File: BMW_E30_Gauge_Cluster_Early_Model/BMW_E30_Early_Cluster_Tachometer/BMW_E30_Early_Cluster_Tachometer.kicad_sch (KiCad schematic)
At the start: 0 parts

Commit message: Started Tach and EG Schematics
Started pinouts for tachometer and EG schematics. Also made a notation update to the Nexus schematic, removed a TODO that was completed.
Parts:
- added D1: 1N4004, Diode_THT:D_DO-41_SOD81_P10.16mm_Horizontal, symbol Diode:1N4005
- added J1: Conn_01x11_Socket, symbol Connector:Conn_01x11_Socket
- added J2: To EG, symbol Connector:Conn_01x05_Socket
- added Q1: BC547C, Package_TO_SOT_THT:TO-92_Inline, symbol Transistor_BJT:BC547
- added R1: 10k, symbol Device:R
- added R2: 20R, symbol Device:R
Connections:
- new net: J1.11 (Pin_11), J2.2 (Pin_2)
- new net: J1.7 (Pin_7), J2.1 (Pin_1)
- new net: D1.1 (K), R2.2
- new net: Q1.2 (B), R1.2
- new net: J2.3 (Pin_3), Q1.1 (C)
- new net +12V T15: D1.2 (A), J1.1 (Pin_1), J2.4 (Pin_4)
- new net +12V T15_ACC: J1.5 (Pin_5)
- new net +12V T30: J1.10 (Pin_10)
- new net +5V: J1.9 (Pin_9)
- new net Cylinder_count: J1.6 (Pin_6), R1.1
- new net GNDPWR: J1.3 (Pin_3), J2.5 (Pin_5), Q1.3 (E)
- new net VCC_T15: R2.1
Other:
- note added: "Cylinder count"
- note added: "Distance pulse"
- note added: "Engine speed input"
- note added: "Fuel rate input"
- note added: "Speed pulse"
- note added: "Wheel speed output"
- company: (none) -> Reagan Ansel
- title: (none) -> BMW E30 Gauge Cluster Tachometer Schematic

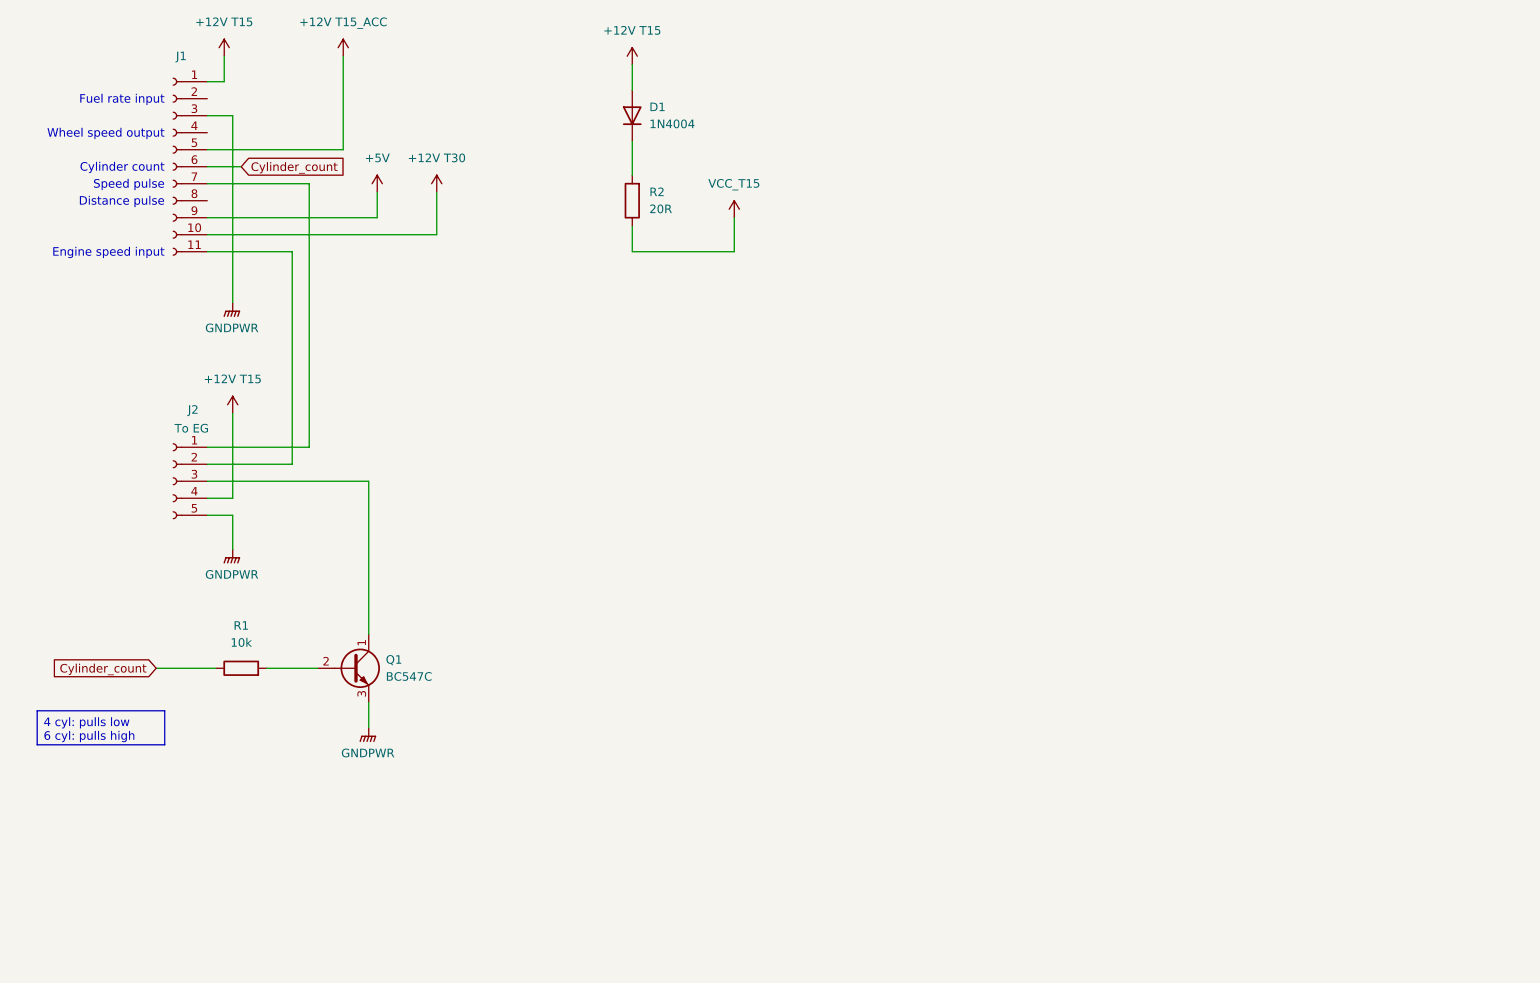
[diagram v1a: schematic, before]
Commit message: Tachometer Schematic Completed
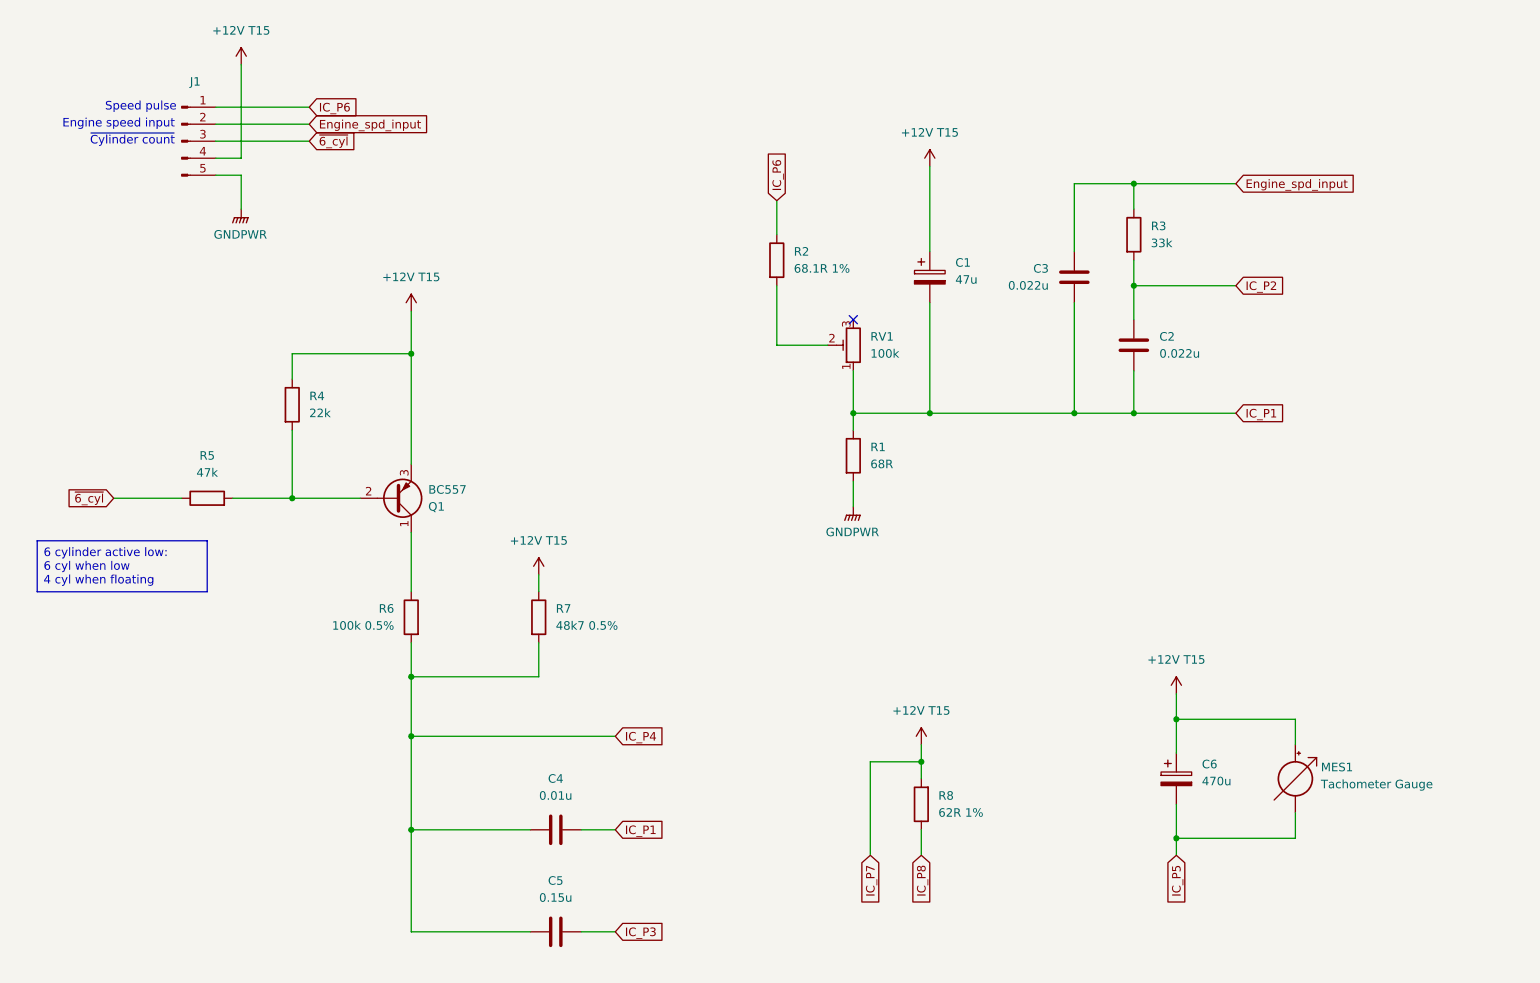
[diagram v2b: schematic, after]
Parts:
- removed D1: 1N4004, Diode_THT:D_DO-41_SOD81_P10.16mm_Horizontal, symbol Diode:1N4005
- removed J1: Conn_01x11_Socket, symbol Connector:Conn_01x11_Socket
- removed J2: To EG, symbol Connector:Conn_01x05_Socket
- removed Q1: BC547C, Package_TO_SOT_THT:TO-92_Inline, symbol Transistor_BJT:BC547
- added C1: 47u, symbol Device:C_Polarized
- added C2, C3: 0.022u, symbol Device:C
- added C4: 0.01u, symbol Device:C
- added C5: 0.15u, symbol Device:C
- added C6: 470u, Capacitor_THT:CP_Axial_L25.0mm_D10.0mm_P30.00mm_Horizontal, symbol Device:C_Polarized
- added J1: Conn_01x05_Pin, symbol Connector:Conn_01x05_Pin
- added MES1: Tachometer Gauge, symbol Device:Galvanometer
- added Q1: BC557, Package_TO_SOT_THT:TO-92_Inline, symbol Transistor_BJT:BC557
- added R3: 33k, symbol Device:R
- added R4: 22k, symbol Device:R
- added R5: 47k, symbol Device:R
- added R6: 100k 0.5%, symbol Device:R
- added R7: 48k7 0.5%, symbol Device:R
- added R8: 62R 1%, symbol Device:R
- added RV1: 100k, Potentiometer_THT:Potentiometer_Runtron_RM-065_Vertical, symbol Device:R_Potentiometer_Trim
- R1: value 10k -> 68R
- R2: value 20R -> 68.1R 1%
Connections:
- net +12V T15: now also C1.1, C6.1, J1.4 (Pin_4), MES1.2 (+), Q1.3 (E), R4.1, R7.1, R8.2
- net GNDPWR: now also R1.2, J1.5 (Pin_5)
- net at R2.2: now also RV1.2
- net Cylinder_count renamed IC_P1
- net IC_P1: now also C1.2, C2.2, C3.2, C4.1, RV1.1
- net VCC_T15 renamed IC_P6
- net IC_P6: now also J1.1 (Pin_1)
- new net: Q1.1 (C), R6.1
- new net: Q1.2 (B), R4.2, R5.2
- new net Engine_spd_input: C3.1, J1.2 (Pin_2), R3.1
- new net IC_P2: C2.1, R3.2
- new net IC_P3: C5.1
- new net IC_P4: C4.2, C5.2, R6.2, R7.2
- new net IC_P5: C6.2, MES1.1 (-)
- new net IC_P8: R8.1
- new net ~{6_cyl}: J1.3 (Pin_3), R5.1
- no-connect marks 0 -> 1
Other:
- note added: "~{Cylinder count}"
- note removed: "Cylinder count"
- note removed: "Distance pulse"
- note removed: "Fuel rate input"
- note removed: "Wheel speed output"
- title: BMW E30 Gauge Cluster Tachometer Schematic -> BMW E30 Gauge Cluster Tachometer Gauge

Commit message: Added IC Symbol
Added symbol for SN29736P to the BMW IC's library and to the schematic.
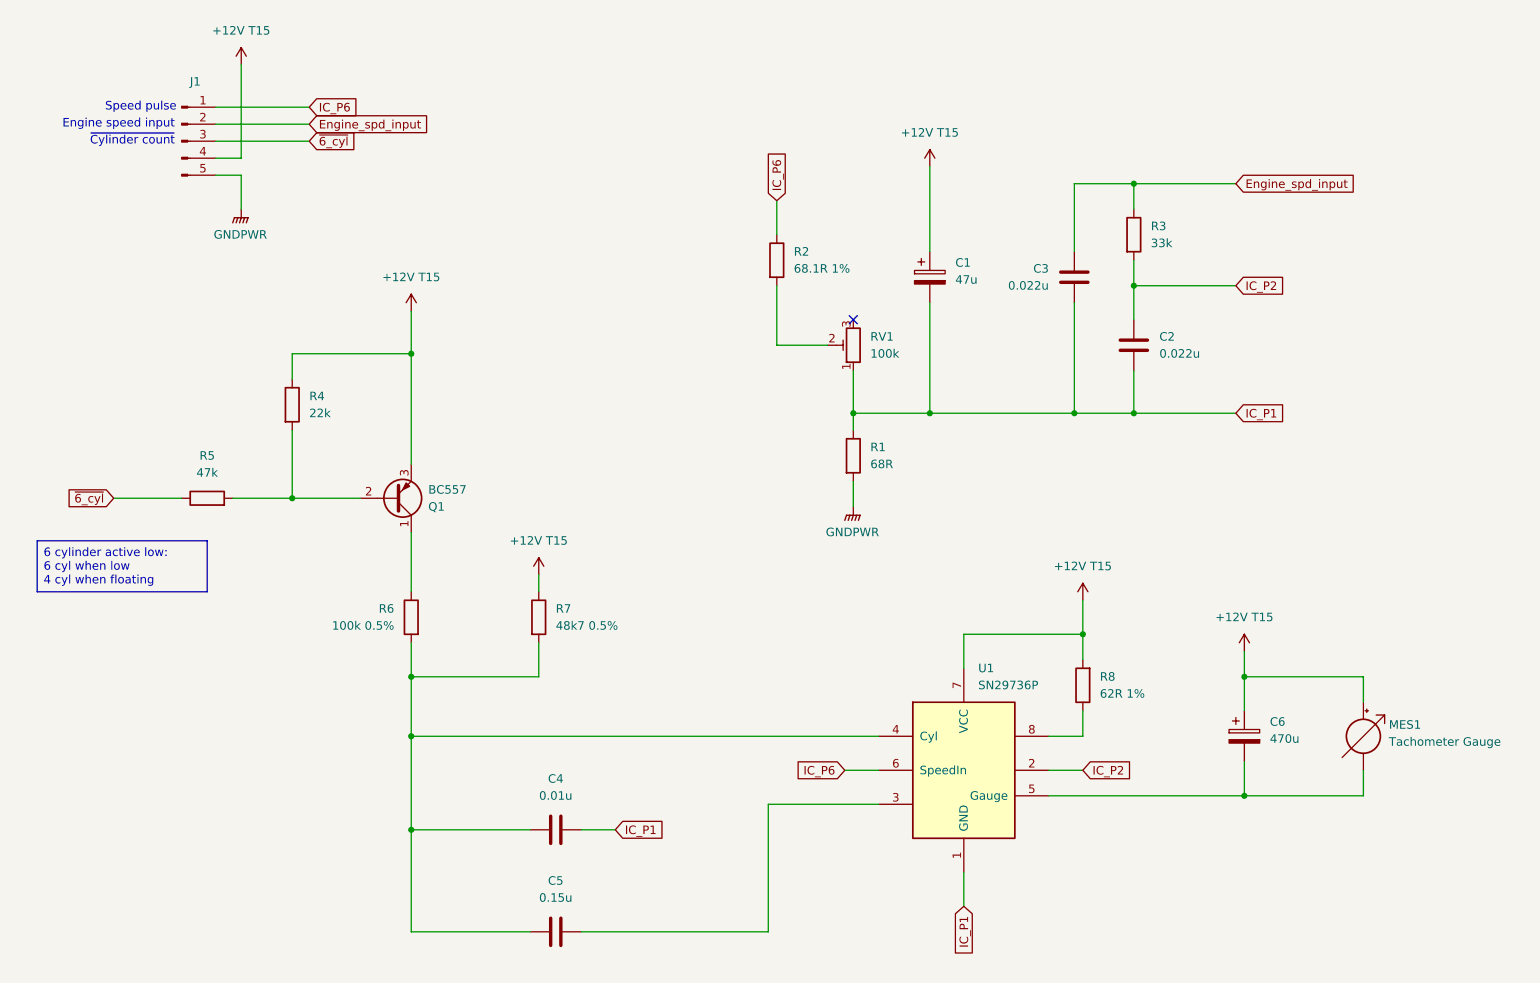
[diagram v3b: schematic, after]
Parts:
- added U1: SN29736P, Package_DIP:DIP-8_W7.62mm_Socket_LongPads, symbol BMW_ICs:SN29736P
- Q1: footprint Package_TO_SOT_THT:TO-92_Inline -> Package_TO_SOT_THT:TO-92_Wide
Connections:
- net +12V T15: now also U1.7 (VCC)
- net IC_P1: now also U1.1 (GND)
- net IC_P2: now also U1.2
- net IC_P6: now also U1.6 (SpeedIn)
- net IC_P3: no longer names the net of C5.1
- net IC_P3: now also U1.3
- net IC_P4: no longer names the net of C4.2, C5.2, R6.2, R7.2
- net IC_P4: now also U1.4 (Cyl)
- net IC_P5: no longer names the net of C6.2, MES1.1 (-)
- net IC_P5: now also U1.5 (Gauge)
- net IC_P8: no longer names the net of R8.1
- net IC_P8: now also U1.8
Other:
- moved on the sheet: C6, MES1, R8

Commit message: Component Placement on Tach Board
Completed component placement part of layout for the tachometer pcb. All footprints are created and locations set. Final step is trace layout.
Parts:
- C1: footprint (none) -> Capacitor_THT:CP_Axial_L11.0mm_D6.0mm_P18.00mm_Horizontal
- C2, C3, C5: footprint (none) -> Capacitor_THT:C_Axial_L12.0mm_D6.5mm_P15.00mm_Horizontal
- C4: footprint (none) -> Capacitor_THT:C_Disc_D5.0mm_W2.5mm_P5.00mm
- J1: footprint (none) -> BMW_Cluster_Connectors:EG_Tach_Pins
- MES1: footprint (none) -> BMW_Cluster_Connectors:Connector_Tach
- R1: footprint (none) -> Resistor_THT:R_Axial_DIN0411_L9.9mm_D3.6mm_P15.24mm_Horizontal
- R2, R3, R4, R5, R6, R7: footprint (none) -> Resistor_THT:R_Axial_DIN0207_L6.3mm_D2.5mm_P7.62mm_Horizontal
- R8: footprint (none) -> Resistor_THT:R_Axial_DIN0309_L9.0mm_D3.2mm_P15.24mm_Horizontal
- RV1: footprint Potentiometer_THT:Potentiometer_Runtron_RM-065_Vertical -> Potentiometer_THT:Potentiometer_Piher_PT-10-V10_Vertical
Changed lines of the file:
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@@
 			)
 		)
-		(property "Footprint" ""
+		(property "Footprint" "Resistor_THT:R_Axial_DIN0207_L6.3mm_D2.5mm_P7.62mm_Horizontal"
 			(at 90.932 107.95 90)
 			(effects
@@
 			)
 		)
-		(property "Footprint" ""
+		(property "Footprint" "Resistor_THT:R_Axial_DIN0207_L6.3mm_D2.5mm_P7.62mm_Horizontal"
 			(at 75.438 107.95 90)
 			(effects
@@
 			)
 		)
-		(property "Footprint" ""
+		(property "Footprint" "Resistor_THT:R_Axial_DIN0207_L6.3mm_D2.5mm_P7.62mm_Horizontal"
 			(at 54.102 76.2 90)
 			(effects
@@
 			)
 		)
-		(property "Footprint" ""
+		(property "Footprint" "BMW_Cluster_Connectors:Connector_Tach"
 			(at 215.9 123.19 90)
 			(effects
@@
 			)
 		)
-		(property "Footprint" ""
+		(property "Footprint" "BMW_Cluster_Connectors:EG_Tach_Pins"
 			(at 39.37 36.83 0)
 			(effects
@@
 			)
 		)
-		(property "Footprint" ""
+		(property "Footprint" "Resistor_THT:R_Axial_DIN0207_L6.3mm_D2.5mm_P7.62mm_Horizontal"
 			(at 43.18 91.948 90)
 			(effects
@@
 			)
 		)
-		(property "Footprint" ""
+		(property "Footprint" "Capacitor_THT:C_Axial_L12.0mm_D6.5mm_P15.00mm_Horizontal"
 			(at 91.44 155.9052 0)
 			(effects
@@
 			)
 		)
-		(property "Footprint" ""
+		(property "Footprint" "Resistor_THT:R_Axial_DIN0207_L6.3mm_D2.5mm_P7.62mm_Horizontal"
 			(at 179.832 50.8 90)
 			(effects
@@
 			)
 		)
-		(property "Footprint" ""
+		(property "Footprint" "Capacitor_THT:C_Disc_D5.0mm_W2.5mm_P5.00mm"
 			(at 91.44 140.6652 0)
 			(effects
@@
 			)
 		)
-		(property "Footprint" ""
+		(property "Footprint" "Resistor_THT:R_Axial_DIN0309_L9.0mm_D3.2mm_P15.24mm_Horizontal"
 			(at 175.768 118.11 90)
 			(effects
@@
 			)
 		)
-		(property "Footprint" ""
+		(property "Footprint" "Capacitor_THT:C_Axial_L12.0mm_D6.5mm_P15.00mm_Horizontal"
 			(at 171.7548 60.96 0)
 			(effects
@@
 			)
 		)
-		(property "Footprint" ""
+		(property "Footprint" "Capacitor_THT:CP_Axial_L11.0mm_D6.0mm_P18.00mm_Horizontal"
 			(at 152.0952 60.96 0)
 			(effects
@@
 			)
 		)
-		(property "Footprint" ""
+		(property "Footprint" "Capacitor_THT:C_Axial_L12.0mm_D6.5mm_P15.00mm_Horizontal"
 			(at 182.5752 71.12 0)
 			(effects
@@
 			)
 		)
-		(property "Footprint" ""
+		(property "Footprint" "Resistor_THT:R_Axial_DIN0411_L9.9mm_D3.6mm_P15.24mm_Horizontal"
 			(at 137.922 83.82 90)
 			(effects
@@
 			)
 		)
-		(property "Footprint" ""
+		(property "Footprint" "Resistor_THT:R_Axial_DIN0207_L6.3mm_D2.5mm_P7.62mm_Horizontal"
 			(at 126.492 54.61 90)
 			(effects
@@
 			)
 		)
-		(property "Footprint" "Potentiometer_THT:Potentiometer_Runtron_RM-065_Vertical"
+		(property "Footprint" "Potentiometer_THT:Potentiometer_Piher_PT-10-V10_Vertical"
 			(at 139.7 67.31 0)
 			(effects

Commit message: Update Schematic PDFs
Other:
- company: Reagan Ansel -> Reans
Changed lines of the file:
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@@
 	(title_block
 		(title "BMW E30 Gauge Cluster Tachometer Gauge")
-		(company "Reagan Ansel")
-		(comment 1 "All resistors are 5% tolorance unless otherwise noted")
+		(date "2026-06-03")
+		(rev "0")
+		(company "Reans")
+		(comment 1 "Reagan Ansel")
+		(comment 2 "All resistors are 5% tolorance unless otherwise noted")
 	)
 	(text "Speed pulse"
@@
 		)
 		(instances
-			(project "BMW_E30_Early_Cluster_EG"
+			(project "BMW_E30_Early_Cluster_Tachometer"
 				(path "/87822f16-f981-4ad2-bfeb-178300c0bdac"
 					(reference "#PWR07")
@@
 		)
 		(instances
-			(project ""
+			(project "BMW_E30_Early_Cluster_Tachometer"
 				(path "/87822f16-f981-4ad2-bfeb-178300c0bdac"
 					(reference "MES1")
@@
 		)
 		(instances
-			(project ""
+			(project "BMW_E30_Early_Cluster_Tachometer"
 				(path "/87822f16-f981-4ad2-bfeb-178300c0bdac"
 					(reference "J1")
@@
 		)
 		(instances
-			(project "BMW_E30_Early_Cluster_EG"
+			(project "BMW_E30_Early_Cluster_Tachometer"
 				(path "/87822f16-f981-4ad2-bfeb-178300c0bdac"
 					(reference "#PWR01")
@@
 		)
 		(instances
-			(project ""
+			(project "BMW_E30_Early_Cluster_Tachometer"
 				(path "/87822f16-f981-4ad2-bfeb-178300c0bdac"
 					(reference "Q1")
@@
 		)
 		(instances
-			(project "BMW_E30_Early_Cluster_EG"
+			(project "BMW_E30_Early_Cluster_Tachometer"
 				(path "/87822f16-f981-4ad2-bfeb-178300c0bdac"
 					(reference "#PWR06")
@@
 		)
 		(instances
-			(project "BMW_E30_Early_Cluster_EG"
+			(project "BMW_E30_Early_Cluster_Tachometer"
 				(path "/87822f16-f981-4ad2-bfeb-178300c0bdac"
 					(reference "R3")
@@
 		)
 		(instances
-			(project "BMW_E30_Early_Cluster_EG"
+			(project "BMW_E30_Early_Cluster_Tachometer"
 				(path "/87822f16-f981-4ad2-bfeb-178300c0bdac"
 					(reference "C3")
@@
 		)
 		(instances
-			(project ""
+			(project "BMW_E30_Early_Cluster_Tachometer"
 				(path "/87822f16-f981-4ad2-bfeb-178300c0bdac"
 					(reference "C1")
@@
 		)
 		(instances
-			(project ""
+			(project "BMW_E30_Early_Cluster_Tachometer"
 				(path "/87822f16-f981-4ad2-bfeb-178300c0bdac"
 					(reference "U1")
@@
 		)
 		(instances
-			(project ""
+			(project "BMW_E30_Early_Cluster_Tachometer"
 				(path "/87822f16-f981-4ad2-bfeb-178300c0bdac"
 					(reference "C2")
@@
 		)
 		(instances
-			(project ""
+			(project "BMW_E30_Early_Cluster_Tachometer"
 				(path "/87822f16-f981-4ad2-bfeb-178300c0bdac"
 					(reference "R1")
@@
 		)
 		(instances
-			(project "BMW_E30_Early_Cluster_EG"
+			(project "BMW_E30_Early_Cluster_Tachometer"
 				(path "/87822f16-f981-4ad2-bfeb-178300c0bdac"
 					(reference "R2")
@@
 		)
 		(instances
-			(project ""
+			(project "BMW_E30_Early_Cluster_Tachometer"
 				(path "/87822f16-f981-4ad2-bfeb-178300c0bdac"
 					(reference "RV1")
@@
 	)
 	(embedded_fonts no)
+	(embedded_files
+		(file
+			(name "reans_sheet_template.kicad_wks")
+			(type worksheet)
+			(data |KLUv/WD/Cu0XAPbhaSEA1TZqxSYVNDoEMnCBWkUAFLHYT8LfLc64wmSW/n9CwQRfAFoAZABfTlM7
+				Cd4PPZP4H186+DUZmyftazMZJC2P8bFwUWq25kUL8mvHwkXR9pEtP+RPAAACHc97OanDZJkyfiu6
+				ZexMnfGD2a9nCIBAQaOUVnXWvtiW2T8EQKDkgCwiGFoOIdn/etgijP3Ss7lq001Ur56Xy2XSChD4
+				izG0r9ol7kx06g/5X/6a1VV7XqJQDq990Dues9+Mwx979pw4IR4v7ePbb9d8i9eDM9hT/3WSxGHt
+				2uJ1q+pJaX8GA4vQjuDbzqhJOcfXfePbr1LR9rtrPIGhJBC7qR8kM8Z09g4omXCSTTKynjjiS1u1
+				q3CTj080beoGpaw+TAqJdN6Eq1gUW6JrkAYXdfWk9EBhnWkl7tsUFo7ieR1p0Ah/UJFzFgWBwsys
+				itUDRWfNENlvxpauoBUjcUhlrs3u12aulxf0XKs+aBalZRWr16FaFa1zTkqrrWV11qovCsPoB+Ee
+				j0iCNBBdsEPihDapC6udeZCNyxjfJvk4juFpWkVZjw3CObqFDYCaoBFNhdgMSQqSFDLMAYBEhObI
+				NmZkXfEEgg31YlRO4GceOtZZSD4tPZJ8rJ74G8PkjH1JKkKawsKGheoJuP2+IlY18ntrNC2s74Pr
+				DVe+cSgd0L7HteZMeDaXmooSSh/c+bVoVTYLk6RKN7Cv2UoaCAZv6YCSS6nbIQTWD7UwQeis5W/V
+				g0dYgB5CyE6HNFbmmlkm5KySJ6yIRrRM5Uc4pc8u9BJFUDGI5kCOG6xadygVBOu2LFloyz3FUwK0
+				K2QvICvncQgSH7pSFluywCLJ0Rwlm2f0GkYN7sFxT4mPYCI2kaL4bSAlPOhlas5v4CmJJDLxSXKn
+				Odp9OHfwRZI7o8xhC2+Z4AAEWT5Rojog0dbMToQXcXHPsDoOuhAAXPmNnp2jRa7V/EUBa9S+lvzC
+				Ux9y2yG0bmId6AOKOjzjaHSplt4lCml0x3i3uxaxGR+0Cg==|
+			)
+			(checksum "582015C87F5C50DCCFBFE692861C814F")
+		)
+	)
 )
